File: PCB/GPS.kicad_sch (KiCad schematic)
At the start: 57 parts, among them J1 5V-36V, J2 Left Header Pins, J3 Right Header Pins, Q1 AO3401A, SW1 SW_Push, SW2 SW_Push, U1 STM32F030C8Tx, U2 TPS5430DDA, U3 SIM808, U4 SMF05CT1G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

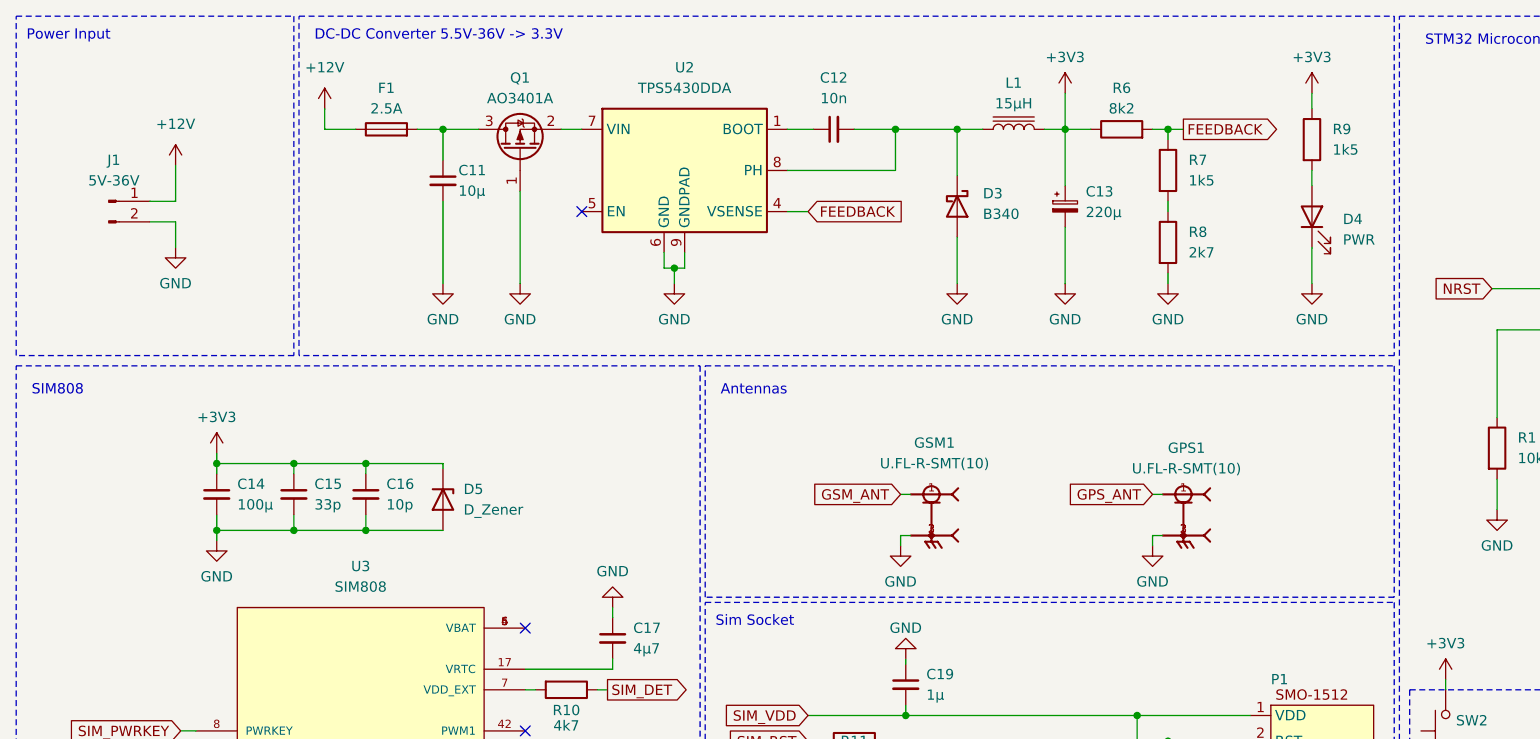
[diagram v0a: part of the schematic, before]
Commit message: Add footprint for all elements
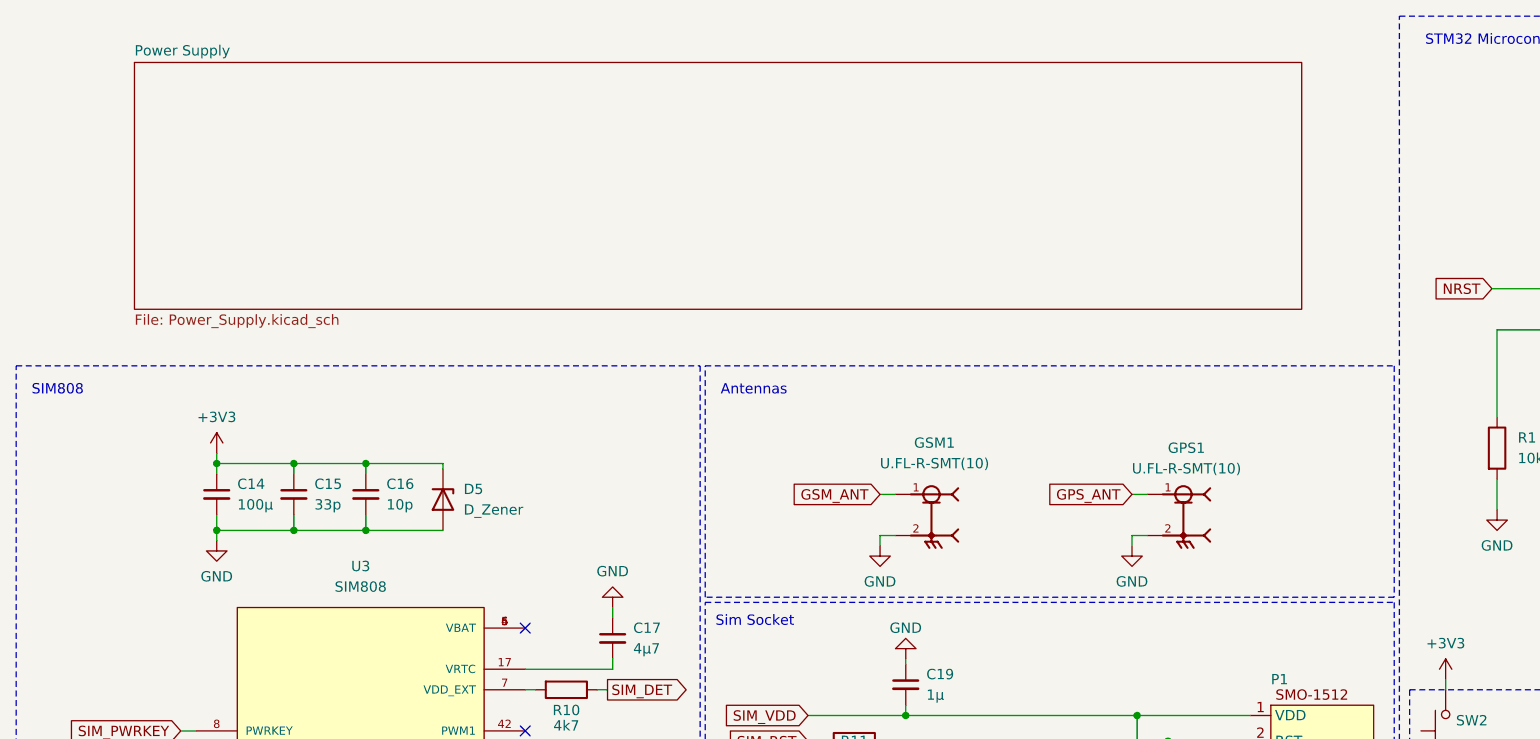
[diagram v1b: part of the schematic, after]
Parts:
- removed C11: 10µ, symbol Device:C_Small
- removed C12: 10n, symbol Device:C_Small
- removed C13: 220µ, symbol Device:C_Polarized_Small
- removed D3: B340, symbol Device:D_Schottky
- removed D4: PWR, symbol Device:LED
- removed F1: 2.5A, symbol Device:Fuse
- removed J1: 5V-36V, symbol Connector:Conn_01x02_Pin
- removed L1: 15µH, symbol Device:L_Iron
- removed Q1: AO3401A, Package_TO_SOT_SMD:SOT-23W_Handsoldering, symbol Transistor_FET:AO3401A
- removed R6: 8k2, symbol Device:R
- removed R7, R9: 1k5, symbol Device:R
- removed R8: 2k7, symbol Device:R
- removed U2: TPS5430DDA, Package_SO:TI_SO-PowerPAD-8_ThermalVias, symbol Regulator_Switching:TPS5430DDA
- C1, C17: footprint (none) -> Capacitor_SMD:C_0603_1608Metric_Pad1.08x0.95mm_HandSolder; LCSC (none) -> C19666
- C10, C2, C3, C4, C5, C6: footprint (none) -> Capacitor_SMD:C_0402_1005Metric_Pad0.74x0.62mm_HandSolder; LCSC (none) -> C1525
- C14: footprint (none) -> Capacitor_SMD:C_1206_3216Metric_Pad1.33x1.80mm_HandSolder; LCSC (none) -> C15008
- C15: footprint (none) -> Capacitor_SMD:C_0402_1005Metric_Pad0.74x0.62mm_HandSolder; LCSC (none) -> C1562
- C16, C9: footprint (none) -> Capacitor_SMD:C_0402_1005Metric_Pad0.74x0.62mm_HandSolder; LCSC (none) -> C32949
- C18: footprint (none) -> Capacitor_SMD:C_0402_1005Metric_Pad0.74x0.62mm_HandSolder; LCSC (none) -> C1555
- C19: footprint (none) -> Capacitor_SMD:C_0402_1005Metric_Pad0.74x0.62mm_HandSolder; LCSC (none) -> C52923
- C7, C8: footprint (none) -> Capacitor_SMD:C_0402_1005Metric_Pad0.74x0.62mm_HandSolder; LCSC (none) -> C1570
- D1: footprint (none) -> LED_SMD:LED_0603_1608Metric_Pad1.05x0.95mm_HandSolder; Color (none) -> Blue; LCSC (none) -> C5151484
- D2: footprint (none) -> LED_SMD:LED_0603_1608Metric_Pad1.05x0.95mm_HandSolder; Color (none) -> Red; LCSC (none) -> C2286
- D5: footprint (none) -> Diode_SMD:D_MiniMELF_Handsoldering; LCSC (none) -> C2857190
- GPS1, GSM1: footprint HRS_U.FL-R-SMT(10) -> Connector_Coaxial:U.FL_Hirose_U.FL-R-SMT-1_Vertical; LCSC (none) -> C88373
- H1, H2, H3, H4: footprint (none) -> MountingHole:MountingHole_2.5mm_Pad_Via; now left out of the parts list
- J2, J3: footprint (none) -> Connector_PinHeader_2.54mm:PinHeader_1x08_P2.54mm_Vertical; now left out of the parts list
- P1: footprint (none) -> Connector_Card:SIM_CARD_SMO-1512; LCSC (none) -> C125621
- R1: footprint (none) -> Resistor_SMD:R_01005_0402Metric_Pad0.57x0.30mm_HandSolder; LCSC (none) -> C25744
- R10: footprint (none) -> Resistor_SMD:R_0402_1005Metric_Pad0.72x0.64mm_HandSolder; LCSC (none) -> C25900
- R11, R12, R13: value R -> 22; footprint (none) -> Resistor_SMD:R_01005_0402Metric_Pad0.57x0.30mm_HandSolder; LCSC (none) -> C25092
- R2: footprint (none) -> Resistor_SMD:R_0201_0603Metric_Pad0.64x0.40mm_HandSolder; LCSC (none) -> C25803
- R3, R4, R5: footprint (none) -> Resistor_SMD:R_0201_0603Metric_Pad0.64x0.40mm_HandSolder; LCSC (none) -> C21190
- SW1, SW2: footprint (none) -> Button_Switch_SMD:XKB-TS-1187A; LCSC (none) -> C318884
- U1: LCSC (none) -> C23922
- U3: footprint XCVR_SIM808 -> MyLibPerso:SIM808; LCSC (none) -> C126275
- U4: footprint SOT65P210X110-6N -> Package_TO_SOT_SMD:SOT-363_SC-70-6_Handsoldering; LCSC (none) -> C15879
- Y1: footprint (none) -> Crystal:Crystal_SMD_5032-2Pin_5.0x3.2mm_HandSoldering; LCSC (none) -> C115962
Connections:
- net GND: no longer GPS1.3, GSM1.3
- no-connect marks 59 -> 58
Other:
- added sheet Power Supply (Power_Supply.kicad_sch)
- note removed: "DC-DC Converter 5.5V-36V -> 3.3V"
- note removed: "Power Input"
